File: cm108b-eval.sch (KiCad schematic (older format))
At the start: 3 parts, among them IC1 CM108B, J1 USB_A

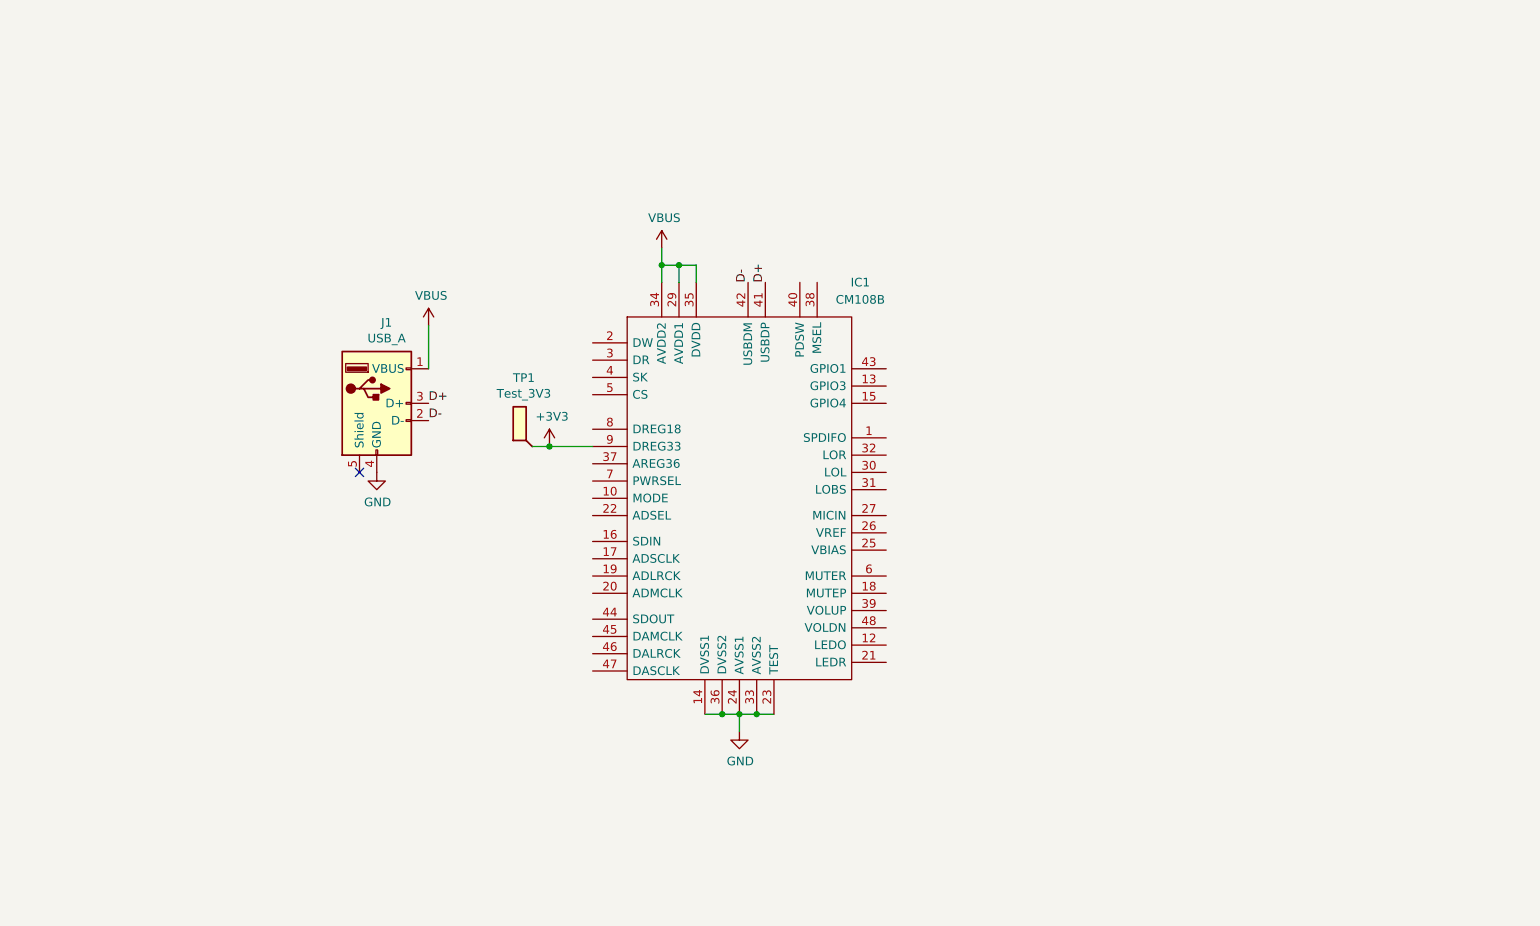
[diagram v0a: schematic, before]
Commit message: Schematic finished
Mostly based on CM108 application note, with changes for CM108B differences. No crystal, no REGV, and I don't know what the LED in J1 is supposed to be.
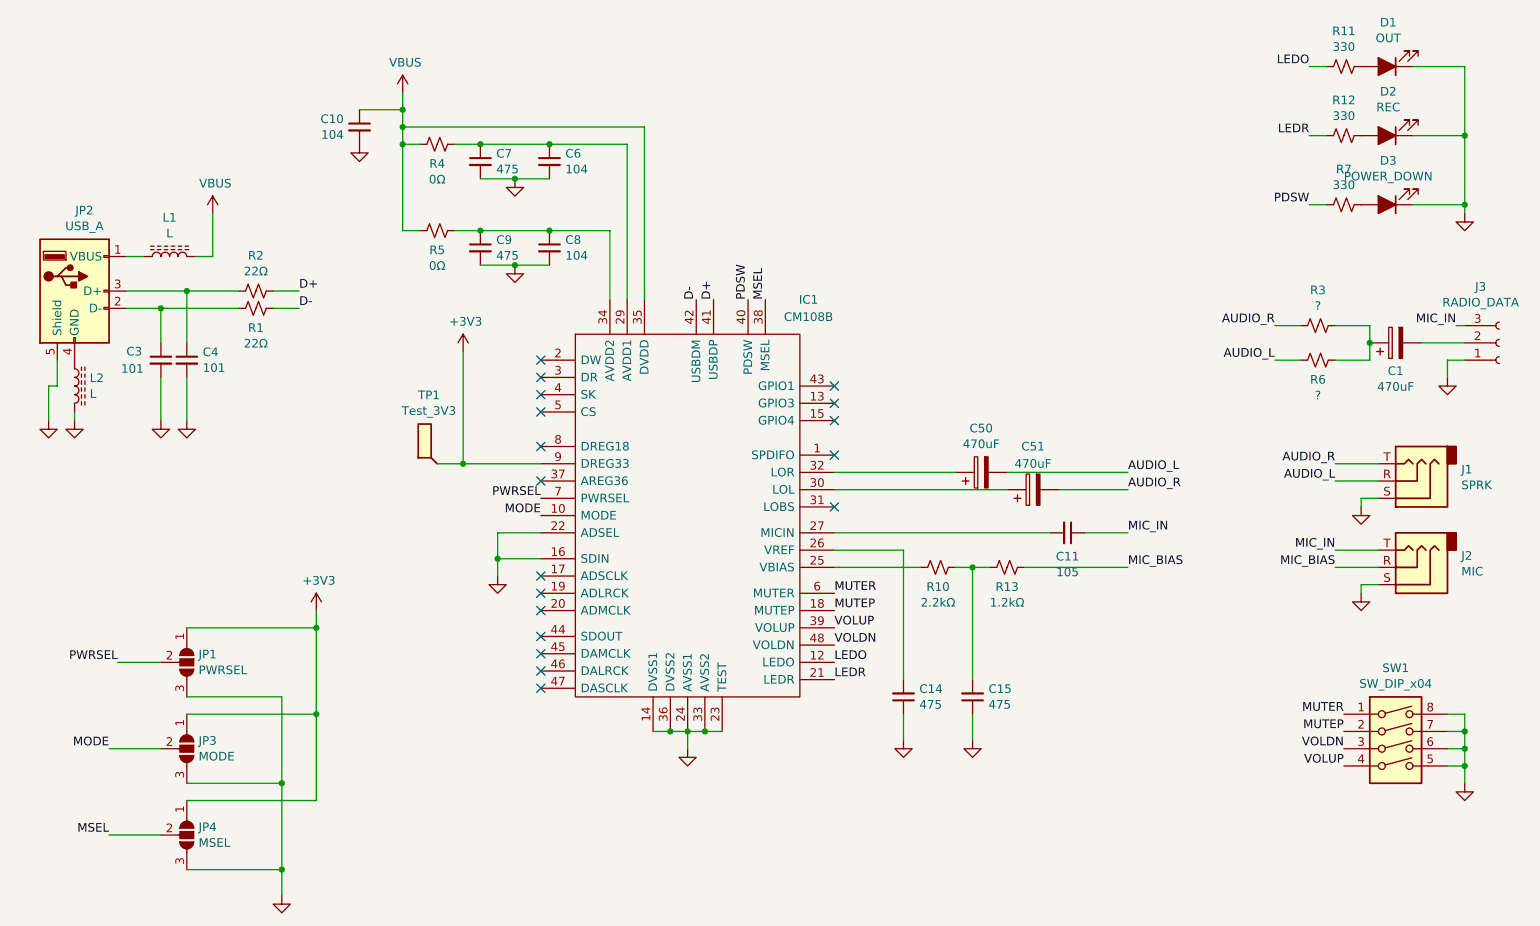
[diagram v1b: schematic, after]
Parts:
- added C1, C50, C51: 470uF, symbol Device:CP
- added C10, C6, C8: 104, symbol Device:C_Small
- added C11: 105, symbol Device:C_Small
- added C14, C15, C7, C9: 475, symbol Device:C_Small
- added C3, C4: 101, symbol Device:C_Small
- added D1: OUT, symbol Device:LED_ALT
- added D2: REC, symbol Device:LED_ALT
- added D3: POWER_DOWN, symbol Device:LED_ALT
- added J1: SPRK, symbol Connector:AudioJack3
- added J2: MIC, symbol Connector:AudioJack3
- added J3: RADIO_DATA, symbol Connector:Conn_01x03_Female
- added JP1: PWRSEL, symbol Jumper:SolderJumper_3_Open
- added JP3: MODE, symbol Jumper:SolderJumper_3_Open
- added JP4: MSEL, symbol Jumper:SolderJumper_3_Open
- added L1, L2: L, symbol Device:L_Core_Ferrite
- added R1, R2: 22Ω, symbol Device:R_Small_US
- added R10: 2.2kΩ, symbol Device:R_Small_US
- added R11, R12, R7: 330, symbol Device:R_Small_US
- added R13: 1.2kΩ, symbol Device:R_Small_US
- added R3, R6: ?, symbol Device:R_Small_US
- added R4, R5: 0Ω, symbol Device:R_Small_US
- added SW1: SW_DIP_x04, symbol Switch:SW_DIP_x04
- renumbered J1 to JP2
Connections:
- net +3V3: now also JP1.1 (A), JP3.1 (A), JP4.1 (A)
- net D+: now also R2.1; no longer JP2.3 (D+)
- net D-: now also R1.1; no longer JP2.2 (D-)
- net GND: now also IC1.16 (SDIN), IC1.22 (ADSEL), JP2.5 (Shield), C10.2, C14.1, C15.1, C3.2, C4.2, C6.2, C7.2, C8.2, C9.2, D1.1 (K), D2.1 (K), D3.1 (K), J1.S, J2.S, J3.1 (Pin_1), JP1.3 (B), JP3.3 (B), JP4.3 (B), L2.2, SW1.5, SW1.6, SW1.7, SW1.8; no longer JP2.4 (GND)
- net VBUS: now also C10.1, L1.2, R4.2, R5.2; no longer IC1.29 (AVDD1), IC1.34 (AVDD2), JP2.1 (VBUS)
- net MODE: now reaches IC1.10 (MODE)
- net MODE: now also JP3.2 (C)
- net LEDO: now reaches IC1.12 (LEDO)
- net LEDO: now also R11.2
- net MUTEP: now reaches IC1.18 (MUTEP)
- net MUTEP: now also SW1.2
- net LEDR: now reaches IC1.21 (LEDR)
- net LEDR: now also R12.2
- net at IC1.25 (VBIAS): now also R10.2
- net at IC1.26 (VREF): now also C14.2
- net at IC1.27 (MICIN): now also C11.2
- net at IC1.30 (LOL): now also C51.1
- net at IC1.32 (LOR): now also C50.1
- net MSEL: now reaches IC1.38 (MSEL)
- net MSEL: now also JP4.2 (C)
- net VOLUP: now reaches IC1.39 (VOLUP)
- net VOLUP: now also SW1.4
- net PDSW: now reaches IC1.40 (PDSW)
- net PDSW: now also R7.2
- net VOLDN: now reaches IC1.48 (VOLDN)
- net VOLDN: now also SW1.3
- net MUTER: now reaches IC1.6 (MUTER)
- net MUTER: now also SW1.1
- net PWRSEL: now reaches IC1.7 (PWRSEL)
- net PWRSEL: now also JP1.2 (C)
- new net: C6.1, C7.1, IC1.29 (AVDD1), R4.1
- new net: C8.1, C9.1, IC1.34 (AVDD2), R5.1
- new net: JP2.1 (VBUS), L1.1
- new net: C3.1, JP2.2 (D-), R1.2
- new net: C4.1, JP2.3 (D+), R2.2
- new net: JP2.4 (GND), L2.1
- new net: D1.2 (A), R11.1
- new net: D2.2 (A), R12.1
- new net: D3.2 (A), R7.1
- new net: C15.2, R10.1, R13.2
- new net: C1.2, J3.2 (Pin_2)
- new net: C1.1, R3.1, R6.1
- new net AUDIO_L: C50.2, J1.R, R6.2
- new net AUDIO_R: C51.2, J1.T, R3.2
- new net MIC_BIAS: J2.R, R13.1
- new net MIC_IN: C11.1, J2.T, J3.3 (Pin_3)
- no-connect marks 1 -> 18
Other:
- moved on the sheet: IC1, JP2, TP1

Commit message: Add schematic
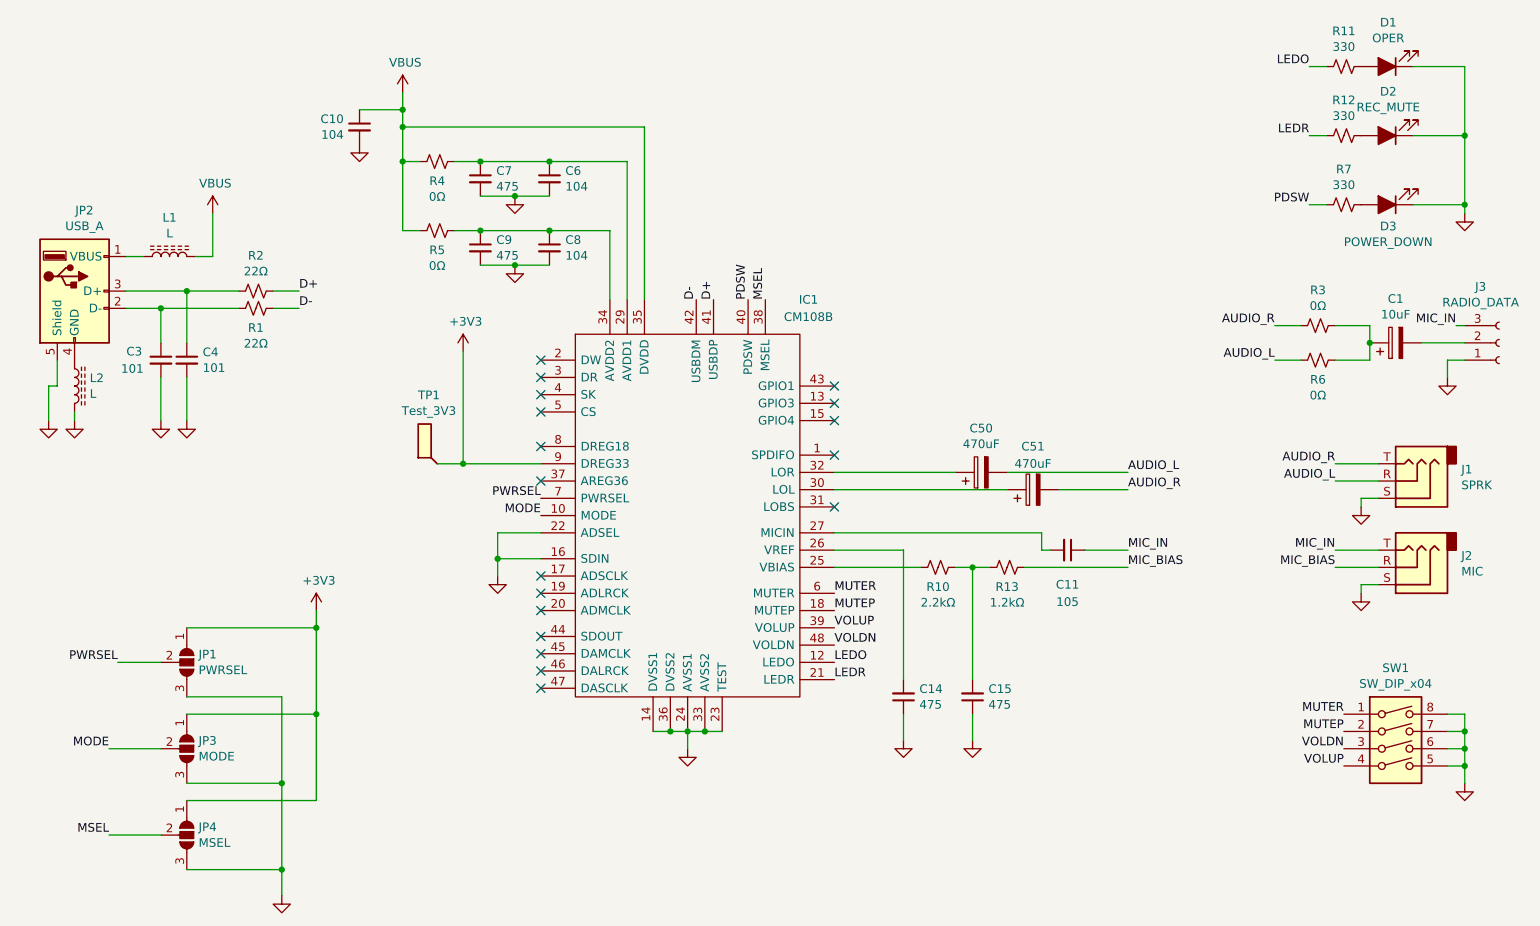
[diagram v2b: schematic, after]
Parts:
- C1: value 470uF -> 10uF
- D1: value OUT -> OPER
- D2: value REC -> REC_MUTE
- R3, R6: value ? -> 0Ω
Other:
- moved on the sheet: C11, C6, C7, R4
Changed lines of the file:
@@
 P 8950 1550
 F 0 "D1" H 8943 1295 50  0000 C CNN
-F 1 "OUT" H 8943 1386 50  0000 C CNN
+F 1 "OPER" H 8943 1386 50  0000 C CNN
 F 2 "" H 8950 1550 50  0001 C CNN
 F 3 "~" H 8950 1550 50  0001 C CNN
@@
 P 8950 1950
 F 0 "D2" H 8943 1695 50  0000 C CNN
-F 1 "REC" H 8943 1786 50  0000 C CNN
+F 1 "REC_MUTE" H 8943 1786 50  0000 C CNN
 F 2 "" H 8950 1950 50  0001 C CNN
 F 3 "~" H 8950 1950 50  0001 C CNN
@@
 U 1 1 606255A6
 P 8950 2350
-F 0 "D3" H 8943 2095 50  0000 C CNN
-F 1 "POWER_DOWN" H 8943 2186 50  0000 C CNN
+F 0 "D3" H 8943 2475 50  0000 C CNN
+F 1 "POWER_DOWN" H 8943 2566 50  0000 C CNN
 F 2 "" H 8950 2350 50  0001 C CNN
 F 3 "~" H 8950 2350 50  0001 C CNN
@@
 	3250 1700 3250 1800
 Wire Wire Line
-	3250 1900 4650 1900
-Wire Wire Line
-	3250 1900 3250 2000
-Wire Wire Line
-	3250 2000 3350 2000
-Connection ~ 3250 1900
+	3250 2100 3350 2100
 $Comp
 L Device:R_Small_US R4
 U 1 1 6066D8B2
-P 3450 2000
-F 0 "R4" V 3563 2000 50  0000 C CNN
-F 1 "0Ω" V 3654 2000 50  0000 C CNN
-F 2 "" H 3450 2000 50  0001 C CNN
-F 3 "~" H 3450 2000 50  0001 C CNN
-	1    3450 2000
-	0    1    1    0
-$EndComp
-Wire Wire Line
-	3550 2000 3700 2000
+P 3450 2100
+F 0 "R4" V 3563 2100 50  0000 C CNN
+F 1 "0Ω" V 3654 2100 50  0000 C CNN
+F 2 "" H 3450 2100 50  0001 C CNN
+F 3 "~" H 3450 2100 50  0001 C CNN
+	1    3450 2100
+	0    1    1    0
+$EndComp
+Wire Wire Line
+	3550 2100 3700 2100
 $Comp
 L Device:C_Small C7
 U 1 1 6066E946
-P 3700 2100
-F 0 "C7" H 3792 2146 50  0000 L CNN
-F 1 "475" H 3792 2055 50  0000 L CNN
-F 2 "" H 3700 2100 50  0001 C CNN
-F 3 "~" H 3700 2100 50  0001 C CNN
-	1    3700 2100
-	1    0    0    -1
-$EndComp
-Connection ~ 3700 2000
-Wire Wire Line
-	3700 2000 4100 2000
+P 3700 2200
+F 0 "C7" H 3792 2246 50  0000 L CNN
+F 1 "475" H 3792 2155 50  0000 L CNN
+F 2 "" H 3700 2200 50  0001 C CNN
+F 3 "~" H 3700 2200 50  0001 C CNN
+	1    3700 2200
+	1    0    0    -1
+$EndComp
+Connection ~ 3700 2100
+Wire Wire Line
+	3700 2100 4100 2100
 $Comp
 L Device:C_Small C6
 U 1 1 6066F351
-P 4100 2100
-F 0 "C6" H 4192 2146 50  0000 L CNN
-F 1 "104" H 4192 2055 50  0000 L CNN
-F 2 "" H 4100 2100 50  0001 C CNN
-F 3 "~" H 4100 2100 50  0001 C CNN
-	1    4100 2100
-	1    0    0    -1
-$EndComp
-Connection ~ 4100 2000
-Wire Wire Line
-	4100 2000 4550 2000
+P 4100 2200
+F 0 "C6" H 4192 2246 50  0000 L CNN
+F 1 "104" H 4192 2155 50  0000 L CNN
+F 2 "" H 4100 2200 50  0001 C CNN
+F 3 "~" H 4100 2200 50  0001 C CNN
+	1    4100 2200
+	1    0    0    -1
+$EndComp
+Connection ~ 4100 2100
+Wire Wire Line
+	4100 2100 4550 2100
 $Comp
 L Device:R_Small_US R5
@@
 Wire Wire Line
 	3350 2500 3250 2500
-Connection ~ 3250 2000
-Wire Wire Line
-	3250 2000 3250 2500
+Connection ~ 3250 2100
+Wire Wire Line
+	3250 2100 3250 2500
 Wire Wire Line
 	4650 1900 4650 2900
-Wire Wire Line
-	4550 2000 4550 2900
 Wire Wire Line
 	4450 2500 4450 2900
@@
 L power:GND #PWR08
 U 1 1 606918F2
-P 3900 2200
-F 0 "#PWR08" H 3900 1950 50  0001 C CNN
-F 1 "GND" H 3905 2027 50  0001 C CNN
-F 2 "" H 3900 2200 50  0001 C CNN
-F 3 "" H 3900 2200 50  0001 C CNN
-	1    3900 2200
-	1    0    0    -1
-$EndComp
-Wire Wire Line
-	3700 2200 3900 2200
-Connection ~ 3900 2200
-Wire Wire Line
-	3900 2200 4100 2200
+P 3900 2300
+F 0 "#PWR08" H 3900 2050 50  0001 C CNN
+F 1 "GND" H 3905 2127 50  0001 C CNN
+F 2 "" H 3900 2300 50  0001 C CNN
+F 3 "" H 3900 2300 50  0001 C CNN
+	1    3900 2300
+	1    0    0    -1
+$EndComp
+Wire Wire Line
+	3700 2300 3900 2300
+Connection ~ 3900 2300
+Wire Wire Line
+	3900 2300 4100 2300
 $Comp
 L power:GND #PWR09
@@
 	1    9100 4450
 	-1   0    0    1
-$EndComp
-$Comp
-L Device:C_Small C11
-U 1 1 606BFEB1
-P 7100 4250
-F 0 "C11" V 7237 4250 50  0000 C CNN
-F 1 "105" V 7328 4250 50  0000 C CNN
-F 2 "" H 7100 4250 50  0001 C CNN
-F 3 "~" H 7100 4250 50  0001 C CNN
-	1    7100 4250
-	0    1    1    0
 $EndComp
 Wire Wire Line
@@
 	7050 4000 7450 4000
 Wire Wire Line
-	7200 4250 7450 4250
-Text Label 7450 4250 0    50   ~ 0
+	7200 4350 7450 4350
+Text Label 7450 4350 0    50   ~ 0
 MIC_IN
 Text Label 7450 4450 0    50   ~ 0
@@
 	8800 4550 8800 4600
 Wire Wire Line
-	5750 4250 7000 4250
-Wire Wire Line
 	6850 4450 7450 4450
 $Comp
@@
 P 8550 3050
 F 0 "R3" V 8345 3050 50  0000 C CNN
-F 1 "?" V 8436 3050 50  0000 C CNN
+F 1 "0Ω" V 8436 3050 50  0000 C CNN
 F 2 "" H 8550 3050 50  0001 C CNN
 F 3 "~" H 8550 3050 50  0001 C CNN
@@
 P 8550 3250
 F 0 "R6" V 8663 3250 50  0000 C CNN
-F 1 "?" V 8754 3250 50  0000 C CNN
+F 1 "0Ω" V 8754 3250 50  0000 C CNN
 F 2 "" H 8550 3250 50  0001 C CNN
 F 3 "~" H 8550 3250 50  0001 C CNN
@@
 U 1 1 6087E15F
 P 9000 3150
-F 0 "C1" V 8837 3150 50  0000 C CNN
-F 1 "470uF" V 8746 3150 50  0000 C CNN
+F 0 "C1" V 9255 3150 50  0000 C CNN
+F 1 "10uF" V 9164 3150 50  0000 C CNN
 F 2 "" H 9038 3000 50  0001 C CNN
 F 3 "~" H 9000 3150 50  0001 C CNN
@@
 Wire Wire Line
 	2150 2650 2150 2400
+Wire Wire Line
+	4550 2100 4550 2900
+Wire Wire Line
+	3250 1900 3250 2100
+Connection ~ 3250 1900
+$Comp
+L Device:C_Small C11
+U 1 1 606BFEB1
+P 7100 4350
+F 0 "C11" V 7300 4350 50  0000 C CNN
+F 1 "105" V 7400 4350 50  0000 C CNN
+F 2 "" H 7100 4350 50  0001 C CNN
+F 3 "~" H 7100 4350 50  0001 C CNN
+	1    7100 4350
+	0    1    1    0
+$EndComp
+Wire Wire Line
+	5750 4250 6950 4250
+Wire Wire Line
+	6950 4250 6950 4350
+Wire Wire Line
+	6950 4350 7000 4350
+Wire Wire Line
+	3250 1900 4650 1900
 $EndSCHEMATC

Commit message: Footprints assigned
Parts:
- removed SW1: SW_DIP_x04, symbol Switch:SW_DIP_x04
- added SW1: MUTE_REC, Button_Switch_SMD:SW_SPST_Omron_B3FS-100xP, symbol Switch:SW_Push
- added SW2: MUTE_PLAY, Button_Switch_SMD:SW_SPST_Omron_B3FS-100xP, symbol Switch:SW_Push
- added SW3: VOL_DN, Button_Switch_SMD:SW_SPST_Omron_B3FS-100xP, symbol Switch:SW_Push
- added SW4: VOL_UP, Button_Switch_SMD:SW_SPST_Omron_B3FS-100xP, symbol Switch:SW_Push
- C1, C10, C11, C14, C15, C3, C4, C6, C7, C8, C9: footprint (none) -> Capacitor_SMD:C_1210_3225Metric
- C50, C51: footprint (none) -> 293D477X9010E2TE3:CAPPM7343X430N; Vendor Part # (none) -> 74-293D477X9010E2TE3
- D1, D2, D3: footprint (none) -> LED_SMD:LED_1210_3225Metric
- J1: footprint (none) -> Connector_Audio:Jack_3.5mm_CUI_SJ-3524-SMT_Horizontal; Vendor Part # (none) -> 490-SJ3524-SMT-TR-GR
- J2: footprint (none) -> Connector_Audio:Jack_3.5mm_CUI_SJ-3524-SMT_Horizontal; Vendor Part # (none) -> 490-SJ3524SMTTRPI
- J3: footprint (none) -> Connector_JST:JST_PH_B3B-PH-SM4-TB_1x03-1MP_P2.00mm_Vertical
- JP1, JP3, JP4: footprint (none) -> Connector_PinHeader_2.54mm:PinHeader_1x03_P2.54mm_Vertical
- L1, L2: footprint (none) -> Inductor_SMD:L_1210_3225Metric
- R1, R10, R11, R12, R13, R2, R3, R4, R5, R6, R7: footprint (none) -> Resistor_SMD:R_1210_3225Metric
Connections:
- net GND: now also SW1.2, SW2.2, SW3.2, SW4.2
- net MUTEP: now also SW2.1
- net MUTER: now also SW1.1
- net VOLDN: now also SW3.1
- net VOLUP: now also SW4.1

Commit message: Change capacitors from exponential notation to units
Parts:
- C11: value 105 -> 1uF
- C14, C15, C7, C9: value 475 -> 4.7uF
- C3, C4: value 101 -> 100pF
- C6, C8: value 104 -> 100nF
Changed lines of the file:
@@
 P 1850 3250
 F 0 "C3" H 1650 3300 50  0000 L CNN
-F 1 "101" H 1750 3200 50  0000 R CNN
+F 1 "100pF" H 1750 3200 50  0000 R CNN
 F 2 "Capacitor_SMD:C_1210_3225Metric" H 1850 3250 50  0001 C CNN
 F 3 "~" H 1850 3250 50  0001 C CNN
@@
 P 2000 3250
 F 0 "C4" H 2092 3296 50  0000 L CNN
-F 1 "101" H 2092 3205 50  0000 L CNN
+F 1 "100pF" H 2092 3205 50  0000 L CNN
 F 2 "Capacitor_SMD:C_1210_3225Metric" H 2000 3250 50  0001 C CNN
 F 3 "~" H 2000 3250 50  0001 C CNN
@@
 Wire Wire Line
 	2000 5800 2750 5800
-Wire Wire Line
-	2750 5800 2750 5300
 Connection ~ 2750 5300
 Wire Wire Line
@@
 Wire Wire Line
 	2000 5200 2550 5200
-Wire Wire Line
-	2550 5200 2550 5700
 Connection ~ 2550 5700
 Wire Wire Line
@@
 P 3700 2200
 F 0 "C7" H 3792 2246 50  0000 L CNN
-F 1 "475" H 3792 2155 50  0000 L CNN
+F 1 "4.7uF" H 3792 2155 50  0000 L CNN
 F 2 "Capacitor_SMD:C_1210_3225Metric" H 3700 2200 50  0001 C CNN
 F 3 "~" H 3700 2200 50  0001 C CNN
@@
 P 4100 2200
 F 0 "C6" H 4192 2246 50  0000 L CNN
-F 1 "104" H 4192 2155 50  0000 L CNN
+F 1 "100nF" H 4192 2155 50  0000 L CNN
 F 2 "Capacitor_SMD:C_1210_3225Metric" H 4100 2200 50  0001 C CNN
 F 3 "~" H 4100 2200 50  0001 C CNN
@@
 P 3700 2600
 F 0 "C9" H 3792 2646 50  0000 L CNN
-F 1 "475" H 3792 2555 50  0000 L CNN
+F 1 "4.7uF" H 3792 2555 50  0000 L CNN
 F 2 "Capacitor_SMD:C_1210_3225Metric" H 3700 2600 50  0001 C CNN
 F 3 "~" H 3700 2600 50  0001 C CNN
@@
 P 4100 2600
 F 0 "C8" H 4192 2646 50  0000 L CNN
-F 1 "104" H 4192 2555 50  0000 L CNN
+F 1 "100nF" H 4192 2555 50  0000 L CNN
 F 2 "Capacitor_SMD:C_1210_3225Metric" H 4100 2600 50  0001 C CNN
 F 3 "~" H 4100 2600 50  0001 C CNN
@@
 P 6150 5200
 F 0 "C14" H 6058 5154 50  0000 R CNN
-F 1 "475" H 6058 5245 50  0000 R CNN
+F 1 "4.7uF" H 6058 5245 50  0000 R CNN
 F 2 "Capacitor_SMD:C_1210_3225Metric" H 6150 5200 50  0001 C CNN
 F 3 "~" H 6150 5200 50  0001 C CNN
@@
 P 6550 5200
 F 0 "C15" H 6458 5154 50  0000 R CNN
-F 1 "475" H 6458 5245 50  0000 R CNN
+F 1 "4.7uF" H 6458 5245 50  0000 R CNN
 F 2 "Capacitor_SMD:C_1210_3225Metric" H 6550 5200 50  0001 C CNN
 F 3 "~" H 6550 5200 50  0001 C CNN
@@
 P 7100 4350
 F 0 "C11" V 6900 4350 50  0000 C CNN
-F 1 "105" V 7000 4350 50  0000 C CNN
+F 1 "1uF" V 7000 4350 50  0000 C CNN
 F 2 "Capacitor_SMD:C_1210_3225Metric" H 7100 4350 50  0001 C CNN
 F 3 "~" H 7100 4350 50  0001 C CNN
@@
 Wire Wire Line
 	8900 5500 8700 5500
+Wire Wire Line
+	2550 4700 2550 5200
+Connection ~ 2550 5200
+Wire Wire Line
+	2550 5200 2550 5700
+Connection ~ 2750 5800
+Wire Wire Line
+	2750 5800 2750 6350
+Wire Wire Line
+	2750 5300 2750 5800
 $EndSCHEMATC

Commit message: PCB laid out
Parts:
- D3: value POWER_DOWN -> PWR_DN
- JP2: footprint usb-a-edge:USB-A_trace -> Connector_USB:USB_Micro-B_Molex_47346-0001
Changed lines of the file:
@@
 F 0 "JP2" H 1407 3317 50  0000 C CNN
 F 1 "USB_A" H 1407 3226 50  0000 C CNN
-F 2 "usb-a-edge:USB-A_trace" H 1500 2800 50  0001 C CNN
+F 2 "Connector_USB:USB_Micro-B_Molex_47346-0001" H 1500 2800 50  0001 C CNN
 F 3 " ~" H 1500 2800 50  0001 C CNN
 	1    1350 2850
@@
 P 8950 2350
 F 0 "D3" H 8943 2475 50  0000 C CNN
-F 1 "POWER_DOWN" H 8943 2566 50  0000 C CNN
+F 1 "PWR_DN" H 8943 2566 50  0000 C CNN
 F 2 "LED_SMD:LED_1210_3225Metric" H 8950 2350 50  0001 C CNN
 F 3 "~" H 8950 2350 50  0001 C CNN
